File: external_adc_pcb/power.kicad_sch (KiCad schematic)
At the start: 12 parts, among them U25 TPS7A2033PDBVR, U26 TLV9061xDBV

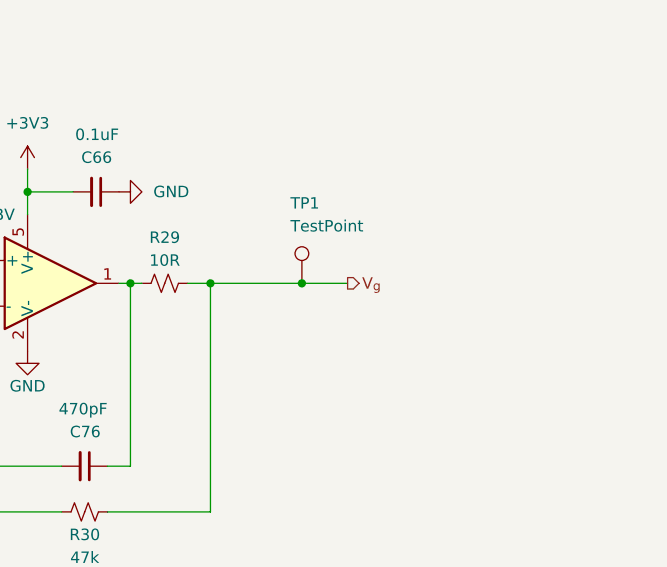
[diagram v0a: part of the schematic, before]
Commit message: capitalize netnames; change and embed font
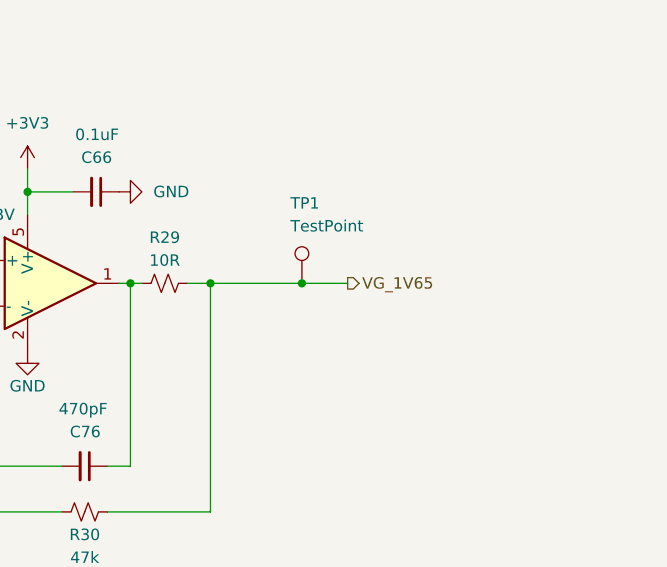
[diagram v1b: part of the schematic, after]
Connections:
- net V_{g} renamed VG_1V65
